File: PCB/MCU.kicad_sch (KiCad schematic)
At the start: 40 parts, among them J1 SWD, Q7 2N7002, Q8 2N7002, Q9 2N7002, SW66 Reset, U2 W25Q128JVS, U3 RP2040, U7 SN74AHCT1G125, Y1 12MHz

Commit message: Large update.
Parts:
- removed C93: 10u, Capacitor_SMD:C_0603_1608Metric, symbol Device:C_Small
- removed C98: 100n, Capacitor_SMD:C_0402_1005Metric, symbol Device:C_Small
- removed D63: 1N4148, Honeydew:D_SOD-323, symbol Device:D_Small
- removed Q7, Q8, Q9: 2N7002, Package_TO_SOT_SMD:SOT-23, symbol Transistor_FET:2N7002
- removed R10: 100k, Resistor_SMD:R_0402_1005Metric, symbol Device:R_Small
- removed R10 (x3), R5: 10k, Resistor_SMD:R_0402_1005Metric, symbol Device:R_Small
- removed R15: 1M, Resistor_SMD:R_0402_1005Metric, symbol Device:R_Small
- removed R20: 1k, Resistor_SMD:R_0402_1005Metric, symbol Device:R_Small
- removed R21: 120k, Resistor_SMD:R_0402_1005Metric, symbol Device:R_Small
- added C96: 100n, Capacitor_SMD:C_0402_1005Metric, symbol Device:C_Small
- added D57: 1N4148, Honeydew:D_SOD-323, symbol Device:D_Small
- added R27 (x2): 10k, Resistor_SMD:R_0402_1005Metric, symbol Device:R_Small
- added SW65: Reset, Button_Switch_SMD:SW_SPDT_PCM12, symbol Cantaloupe:SW_SPST_Small
- C10, C5, C6, C9: Voltage (none) -> 50V
- C11, C12, C13, C14, C15, C16, C17, C18, C19, C7, C8, C92: LCSC C1525 -> C307331; Voltage (none) -> 50V
- J1: footprint Honeydew:PinHeader_1x04_P2.54mm_Vertical_SIlkless -> Connector_PinHeader_2.54mm:PinHeader_1x03_P2.54mm_Vertical; symbol Connector_Generic:Conn_01x04 -> Connector_Generic:Conn_01x03
- SW66: footprint Button_Switch_SMD:SW_SPST_TL3342 -> Honeydew:Panasonic_EVQPUL_EVQPUC; LCSC C318884 -> C79174
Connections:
- net +3V3: now also D57.1 (K), R27.1, R27.1; no longer J1.4 (Pin_4), R6.1, SW66.2 (B)
- net DC_OLED: now also U3.38 (GPIO26_ADC0); no longer U3.40 (GPIO28_ADC2)
- net GND: now also SW66.1 (A), C96.1, SW65.1 (A)
- net RX: now also U3.40 (GPIO28_ADC2); no longer U3.38 (GPIO26_ADC0)
- net SS_OLED: now also U3.39 (GPIO27_ADC1); no longer U3.41 (GPIO29_ADC3)
- net TX: now also U3.41 (GPIO29_ADC3); no longer U3.39 (GPIO27_ADC1)
- net ~{RST}: now also SW66.2 (B), C96.2, D57.2 (A), R27.2; no longer R6.2
- net +5V renamed +5VD
- net COL12 renamed COLM
- net Flash_SS: no longer names the net of U2.1 (~{CS}), U3.56 (QSPI_SS)
- net Flash_SS: now also R6.1, R27.2
- new net: R6.2, SW65.2 (B)
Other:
- moved on the sheet: C10, C5, C6, C9, R7, R8, R9, SW66, U2, U3, U7, Y1

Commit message: Added large caps to output of TPS2557. Updated STEP file and file data.
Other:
- company: (none) -> Created by Ariamelon (https://github.com/Ariamelon/Honeydew/)
- title: (none) -> Honeydew unified split ergonomic keyboard
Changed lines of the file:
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@@
   (paper "A4")
   (title_block
-    (date "2023-04-03")
+    (title "Honeydew unified split ergonomic keyboard")
+    (date "2023-04-08")
     (rev "V2.0")
+    (company "Created by Ariamelon (https://github.com/Ariamelon/Honeydew/)")
     (comment 1 "All capacitors 50V unless otherwise specified.")
+    (comment 2 "Licensed under CC BY 4.0.")
   )
   (junction (at 146.05 31.75) (diameter 0) (color 0 0 0 0)

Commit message: Added plate DXF and gerbers. Removed split comms ports and ideal diode.
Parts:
- SW66: LCSC C79174 -> C110293
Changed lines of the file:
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@@
       (effects (font (size 1.27 1.27)) hide)
     )
-    (property "LCSC" "C79174" (at 181.61 85.09 0)
+    (property "LCSC" "C110293" (at 181.61 85.09 0)
       (effects (font (size 1.27 1.27)) hide)
     )

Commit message: 17/04/2023 large update.
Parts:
- removed C11, C92, C96: 100n, Capacitor_SMD:C_0402_1005Metric, symbol Device:C_Small
- removed SW65: Reset, Button_Switch_SMD:SW_SPDT_PCM12, symbol Cantaloupe:SW_SPST_Small
- removed SW66: Reset, Honeydew:Panasonic_EVQPUL_EVQPUC, symbol Cantaloupe:SW_SPST_Small
- removed U7: SN74AHCT1G125, Package_TO_SOT_SMD:SOT-23-5, symbol Honeydew:SN74AHCT1G125
- added C101: 4u7, Capacitor_SMD:C_0603_1608Metric, symbol Device:C_Small
- added C24, C25: 100n, Capacitor_SMD:C_0402_1005Metric, symbol Device:C_Small
- added SW68: Reset, Honeydew:Panasonic_EVQPUL_EVQPUC, symbol Cantaloupe:SW_SPST_Small
- added SW69: BOOT_SEL, Button_Switch_SMD:SW_SPDT_PCM12, symbol Switch:SW_SPDT
- added U3: SN74AHCT1G125, Package_TO_SOT_SMD:SOT-23-5, symbol Honeydew:SN74AHCT1G125
- J1: footprint Connector_PinHeader_2.54mm:PinHeader_1x03_P2.54mm_Vertical -> Honeydew:Header_SWD
- U2: footprint Package_SO:SOIC-8_5.23x5.23mm_P1.27mm -> Honeydew:SOIC-8_5.23x5.23mm_P1.27mm
- renumbered C10 to C11, U3 to U1
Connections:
- net COLM is gone; now on net ROW2: U1.14 (GPIO11)
- net MOTION is gone; now on net ROW4: U1.16 (GPIO13)
- net +3V3: now also C101.2, C25.2
- net GND: now also C101.1, C24.1, C25.1, SW68.1 (A), SW69.2 (B), SW69.3 (C), U3.1 (~{OE}), U3.3 (GND)
- net RGB: now also U3.4 (Y)
- net ROW0: now also U1.12 (GPIO9); no longer U1.8 (GPIO6)
- net ROW1: now also U1.13 (GPIO10); no longer U1.9 (GPIO7)
- net ROW2: no longer U1.11 (GPIO8)
- net ROW3: now also U1.15 (GPIO12); no longer U1.12 (GPIO9)
- net ROW4: no longer U1.13 (GPIO10)
- net ~{RST}: now also C24.2, SW68.2 (B)
- net FLASH_CS: now reaches R27.2, R6.1, U1.56 (QSPI_SS), U2.1 (~{CS})
- net FLASH_SD1: now reaches U1.55 (QSPI_SD1), U2.2 (DO(IO1))
- net FLASH_SD2: now reaches U1.54 (QSPI_SD2), U2.3 (IO2)
- net FLASH_SD0: now reaches U1.53 (QSPI_SD0), U2.5 (DI(IO0))
- net FLASH_CLK: now reaches U1.52 (QSPI_SCLK), U2.6 (CLK)
- net FLASH_SD3: now reaches U1.51 (QSPI_SD3), U2.7 (IO3)
- net at R6.2: now also SW69.1 (A)
- net SWD: now reaches J1.1 (Pin_1), U1.25 (SWD)
- net SWC: now reaches J1.3 (Pin_3), U1.24 (SWCLK)
- net COL0 renamed 1500mA_EN
- net COL1 renamed 3000mA_EN
- net COL10: no longer names the net of U1.3 (GPIO1)
- net COL11 renamed RGB_3V3
- net RGB_3V3: now also U3.2 (A)
- net COL2 renamed OLED_CS
- net COL3 renamed OLED_DC
- net COL4 renamed TB_CS
- net COL5 renamed TB_MOT
- net COL6: no longer names the net of U1.7 (GPIO5)
- net COL7: no longer names the net of U1.6 (GPIO4)
- net COL8: no longer names the net of U1.5 (GPIO3)
- net COL9: no longer names the net of U1.4 (GPIO2)
- net DC_OLED renamed I_SEN
- net RX renamed TUSB_OUT2
- net SS_OLED renamed ILIM_~{FLT}
- net SS_TB renamed MATRIX_CS
- net TX renamed TUSB_OUT1
- new net +5V: U3.5 (VCC)
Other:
- moved on the sheet: C11, J1, R27, R6

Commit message: Rerouting.
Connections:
- net ROTA: now also U1.8 (GPIO6); no longer U1.17 (GPIO14)
- net ROTB: now also U1.9 (GPIO7); no longer U1.18 (GPIO15)
- net ROW0: now also U1.3 (GPIO1); no longer U1.12 (GPIO9)
- net ROW1: now also U1.4 (GPIO2); no longer U1.13 (GPIO10)
- net ROW2: now also U1.5 (GPIO3); no longer U1.14 (GPIO11)
- net ROW3: now also U1.6 (GPIO4); no longer U1.15 (GPIO12)
- net ROW4: now also U1.7 (GPIO5); no longer U1.16 (GPIO13)
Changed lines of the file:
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@@
     (stroke (width 0) (type default))
   )
-  (wire (pts (xy 130.81 76.2) (xy 128.27 76.2))
+  (wire (pts (xy 130.81 55.88) (xy 128.27 55.88))
     (stroke (width 0) (type default))
   )
@@
     (stroke (width 0) (type default))
   )
-  (wire (pts (xy 130.81 71.12) (xy 128.27 71.12))
+  (wire (pts (xy 130.81 50.8) (xy 128.27 50.8))
     (stroke (width 0) (type default))
   )
@@
     (stroke (width 0) (type default))
   )
-  (wire (pts (xy 130.81 86.36) (xy 128.27 86.36))
+  (wire (pts (xy 130.81 66.04) (xy 128.27 66.04))
     (stroke (width 0) (type default))
   )
@@
     (stroke (width 0) (type default))
   )
-  (wire (pts (xy 130.81 83.82) (xy 128.27 83.82))
+  (wire (pts (xy 130.81 63.5) (xy 128.27 63.5))
     (stroke (width 0) (type default))
   )
@@
     (stroke (width 0) (type default))
   )
-  (wire (pts (xy 130.81 73.66) (xy 128.27 73.66))
+  (wire (pts (xy 130.81 53.34) (xy 128.27 53.34))
     (stroke (width 0) (type default))
   )
@@
     (stroke (width 0) (type default))
   )
-  (wire (pts (xy 130.81 78.74) (xy 128.27 78.74))
+  (wire (pts (xy 130.81 58.42) (xy 128.27 58.42))
     (stroke (width 0) (type default))
   )
@@
     (stroke (width 0) (type default))
   )
-  (wire (pts (xy 130.81 81.28) (xy 128.27 81.28))
+  (wire (pts (xy 130.81 60.96) (xy 128.27 60.96))
     (stroke (width 0) (type default))
   )
@@
     )
   )
-  (hierarchical_label "ROW1" (shape input) (at 130.81 73.66 0) (fields_autoplaced)
+  (hierarchical_label "ROW1" (shape input) (at 130.81 53.34 0) (fields_autoplaced)
     (effects (font (size 1.27 1.27)) (justify left))
   )
@@
     (effects (font (size 1.27 1.27)) (justify left))
   )
-  (hierarchical_label "ROW3" (shape input) (at 130.81 78.74 0) (fields_autoplaced)
+  (hierarchical_label "ROW3" (shape input) (at 130.81 58.42 0) (fields_autoplaced)
     (effects (font (size 1.27 1.27)) (justify left))
   )
@@
     (effects (font (size 1.27 1.27)) (justify left))
   )
-  (hierarchical_label "ROTB" (shape output) (at 130.81 86.36 0) (fields_autoplaced)
-    (effects (font (size 1.27 1.27)) (justify left))
-  )
-  (hierarchical_label "ROTA" (shape output) (at 130.81 83.82 0) (fields_autoplaced)
+  (hierarchical_label "ROTB" (shape output) (at 130.81 66.04 0) (fields_autoplaced)
+    (effects (font (size 1.27 1.27)) (justify left))
+  )
+  (hierarchical_label "ROTA" (shape output) (at 130.81 63.5 0) (fields_autoplaced)
     (effects (font (size 1.27 1.27)) (justify left))
   )
@@
     (effects (font (size 1.27 1.27)) (justify left))
   )
-  (hierarchical_label "ROW2" (shape input) (at 130.81 76.2 0) (fields_autoplaced)
+  (hierarchical_label "ROW2" (shape input) (at 130.81 55.88 0) (fields_autoplaced)
     (effects (font (size 1.27 1.27)) (justify left))
   )
@@
     (effects (font (size 1.27 1.27)) (justify left))
   )
-  (hierarchical_label "ROW4" (shape input) (at 130.81 81.28 0) (fields_autoplaced)
+  (hierarchical_label "ROW4" (shape input) (at 130.81 60.96 0) (fields_autoplaced)
     (effects (font (size 1.27 1.27)) (justify left))
   )
@@
     (effects (font (size 1.27 1.27)) (justify left))
   )
-  (hierarchical_label "ROW0" (shape input) (at 130.81 71.12 0) (fields_autoplaced)
-    (effects (font (size 1.27 1.27)) (justify left))
-  )
+  (hierarchical_label "ROW0" (shape input) (at 130.81 50.8 0) (fields_autoplaced)
+    (effects (font (size 1.27 1.27)) (justify left))
+  )

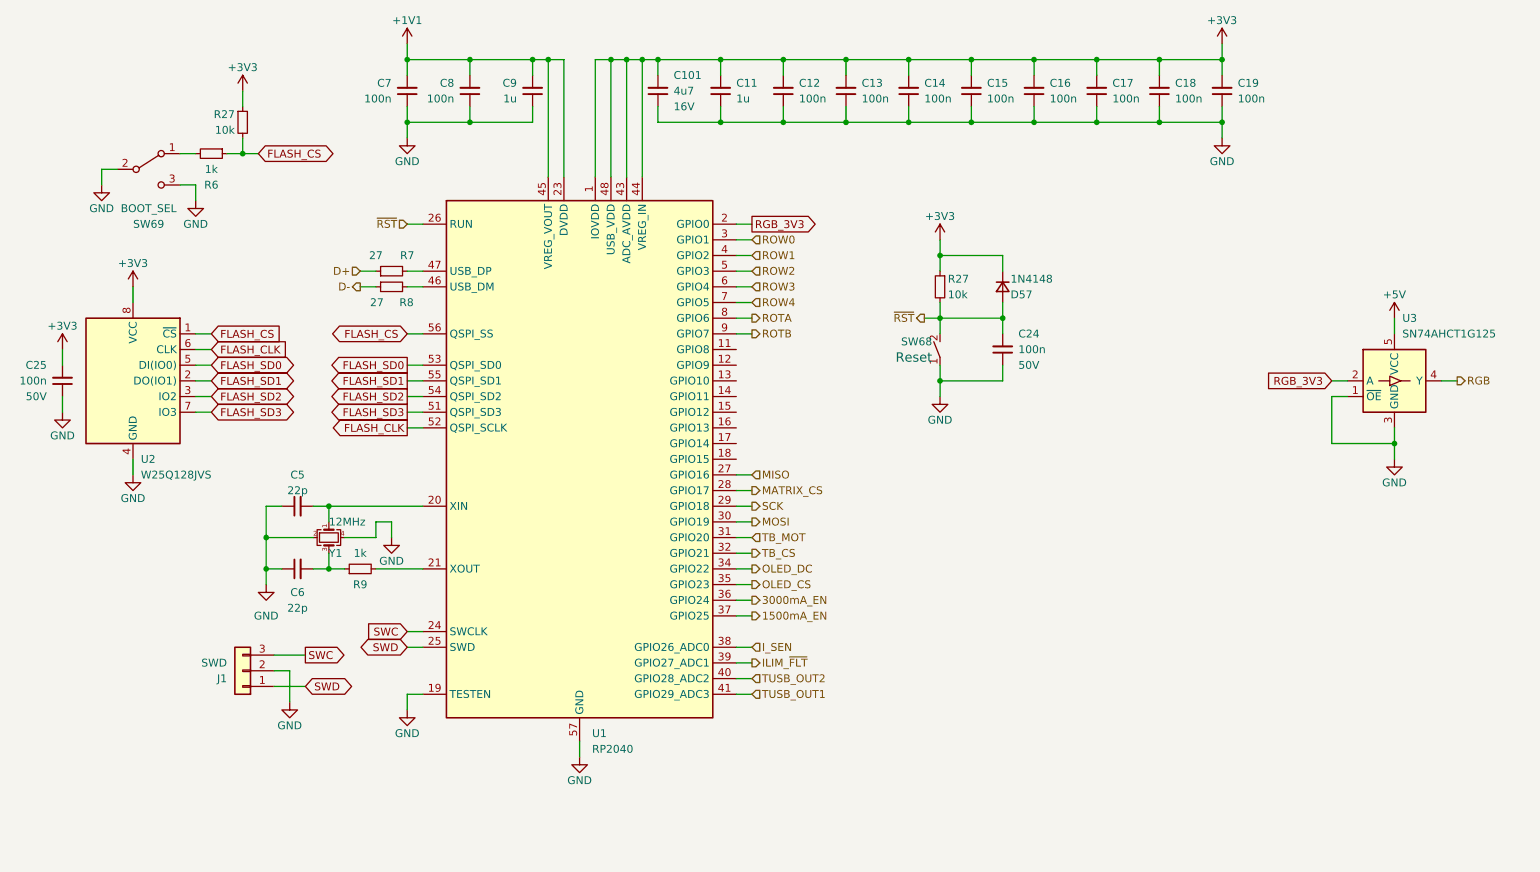
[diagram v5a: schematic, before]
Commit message: 3/4-done update.
Added current and voltage measurement for VBUS in and current measurement for the RGB output. Added PMOS power switch to fully turn off RGB LEDs when not in use. Rerouted the PCB. Moved OLED ribbon cable cutout and expanded it length-wise. Changed position of various components for better routing. Changed bulk capacitance of RGB LEDs to 5 x 22u capacitors. Changed the four N mosfets to two much smaller dual N mosfets. Still need to do RGB routing!
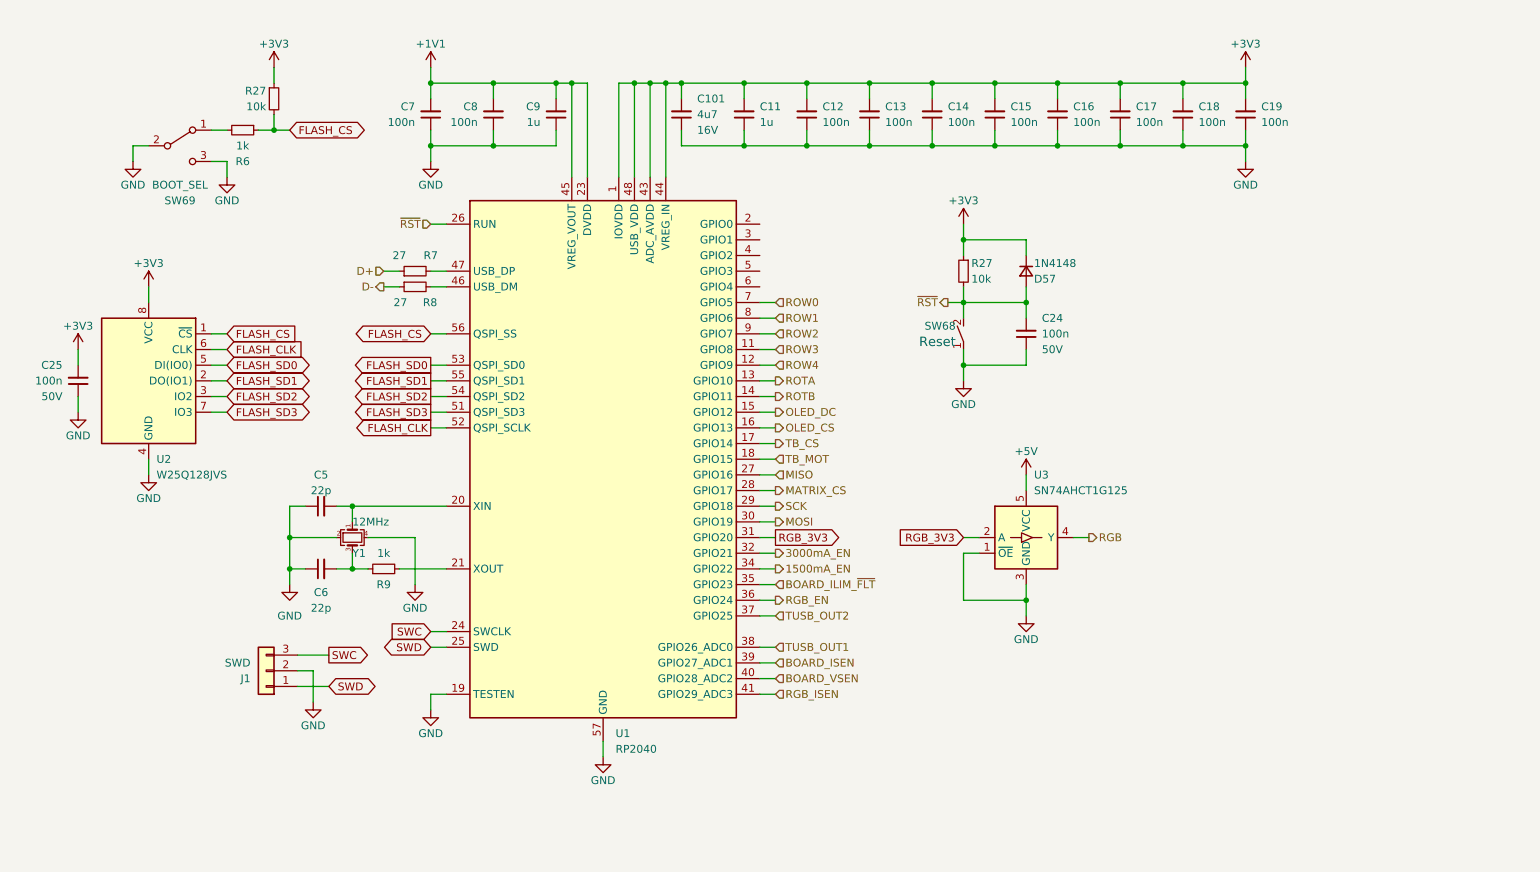
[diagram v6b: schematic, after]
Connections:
- net I_SEN is gone; now on net TUSB_OUT1: U1.38 (GPIO26_ADC0)
- net 1500mA_EN: now also U1.34 (GPIO22); no longer U1.37 (GPIO25)
- net 3000mA_EN: now also U1.32 (GPIO21); no longer U1.36 (GPIO24)
- net OLED_CS: now also U1.16 (GPIO13); no longer U1.35 (GPIO23)
- net OLED_DC: now also U1.15 (GPIO12); no longer U1.34 (GPIO22)
- net RGB_3V3: now also U1.31 (GPIO20); no longer U1.2 (GPIO0)
- net ROTA: now also U1.13 (GPIO10); no longer U1.8 (GPIO6)
- net ROTB: now also U1.14 (GPIO11); no longer U1.9 (GPIO7)
- net ROW0: now also U1.7 (GPIO5); no longer U1.3 (GPIO1)
- net ROW1: now also U1.8 (GPIO6); no longer U1.4 (GPIO2)
- net ROW2: now also U1.9 (GPIO7); no longer U1.5 (GPIO3)
- net ROW3: now also U1.11 (GPIO8); no longer U1.6 (GPIO4)
- net ROW4: now also U1.12 (GPIO9); no longer U1.7 (GPIO5)
- net TB_CS: now also U1.17 (GPIO14); no longer U1.32 (GPIO21)
- net TB_MOT: now also U1.18 (GPIO15); no longer U1.31 (GPIO20)
- net TUSB_OUT1: no longer U1.41 (GPIO29_ADC3)
- net TUSB_OUT2: now also U1.37 (GPIO25); no longer U1.40 (GPIO28_ADC2)
- net ILIM_~{FLT} renamed BOARD_ISEN
- new net BOARD_ILIM_~{FLT}: U1.35 (GPIO23)
- new net BOARD_VSEN: U1.40 (GPIO28_ADC2)
- new net RGB_EN: U1.36 (GPIO24)
- new net RGB_ISEN: U1.41 (GPIO29_ADC3)
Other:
- moved on the sheet: C101, C11, C12, C13, C14, C15, C16, C17, C18, C19, C24, C25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

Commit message: BLE version incomplete update.
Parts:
- removed C101: 4u7, Capacitor_SMD:C_0603_1608Metric, symbol Device:C_Small
- removed C12, C13, C14, C15, C16, C17, C18, C19, C25, C7, C8: 100n, Capacitor_SMD:C_0402_1005Metric, symbol Device:C_Small
- removed C9: 1u, Capacitor_SMD:C_0603_1608Metric, symbol Device:C_Small
- removed J1: SWD, Honeydew:Header_SWD, symbol Connector_Generic:Conn_01x03
- removed R27 (x2): 10k, Resistor_SMD:R_0402_1005Metric, symbol Device:R_Small
- removed R6, R9: 1k, Resistor_SMD:R_0402_1005Metric, symbol Device:R_Small
- removed R7, R8: 27, Resistor_SMD:R_0402_1005Metric, symbol Device:R_Small
- removed SW69: BOOT_SEL, Button_Switch_SMD:SW_SPDT_PCM12, symbol Switch:SW_SPDT
- removed U1: RP2040, Honeydew:QFN-56-1EP_7x7mm_P0.4mm_EP3.2x3.2mm_ThermalVias, symbol MCU_RaspberryPi:RP2040
- removed U2: W25Q128JVS, Honeydew:SOIC-8_5.23x5.23mm_P1.27mm, symbol Memory_Flash:W25Q128JVS
- removed U3: SN74AHCT1G125, Package_TO_SOT_SMD:SOT-23-5, symbol Honeydew:SN74AHCT1G125
- removed Y1: 12MHz, Crystal:Crystal_SMD_3225-4Pin_3.2x2.5mm, symbol Device:Crystal_GND24_Small
- added C28: 100n, Capacitor_SMD:C_0402_1005Metric, symbol Device:C_Small
- added C31: 4u7, Capacitor_SMD:C_0603_1608Metric, symbol Device:C_Small
- added C39 (x2): 10u, Capacitor_SMD:C_0603_1608Metric, symbol Device:C_Small
- added D65: SK6805, LED_SMD:LED_SK6805_PLCC4_2.4x2.7mm_P1.3mm, symbol LED:SK6805
- added J6: SWD, Connector_PinHeader_1.27mm:PinHeader_2x05_P1.27mm_Vertical, symbol Connector_Generic:Conn_02x05_Odd_Even
- added Q1: BSS138BKS, Package_TO_SOT_SMD:SOT-363_SC-70-6, symbol Device:Q_Dual_NMOS_S1G1D2S2G2D1
- added Q4: AON7407, Honeydew:AO_DFN-8-3x3, symbol Transistor_FET:AON6411
- added R16: 1k, Resistor_SMD:R_0402_1005Metric, symbol Device:R_Small
- added R32 (x2): 10k, Resistor_SMD:R_0402_1005Metric, symbol Device:R_Small
- added U1: MDBT50Q-U1MV2, RF_Module:Raytac_MDBT50Q, symbol Honeydew:MDBT50Q
- added U3: W25Q128JW, Package_SON:WSON-8-1EP_6x5mm_P1.27mm_EP3.4x4.3mm, symbol Memory_Flash:W25Q32JVZP
- added U6: SN74LV1T34, Package_TO_SOT_SMD:SOT-353_SC-70-5, symbol Logic_LevelTranslator:SN74LV1T34DCK
- added Y1: 32.768k, Crystal:Crystal_SMD_3215-2Pin_3.2x1.5mm, symbol Device:Crystal_Small
- C11: value 1u -> 100n; footprint Capacitor_SMD:C_0603_1608Metric -> Capacitor_SMD:C_0402_1005Metric; LCSC C15849 -> C307331
- C5, C6: value 22p -> 15p; LCSC C1555 -> C1548
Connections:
- net GND: now also C28.1, C39.2, C39.2, D65.2 (VSS), J6.3 (Pin_3), J6.5 (Pin_5), J6.9 (Pin_9), Q1.4 (S), U1.1 (GND), U1.15 (GND), U1.2 (GND), U1.33 (GND), U1.55 (GND), U3.4 (GND), U3.9 (EP), U6.3 (GND)
- net RGB_EN: now also Q1.5 (G)
- net ~{RST}: now also J6.10 (Pin_10), R32.2, U1.40 (~{RESET}/P0.18)
- net at C6.2: now also U1.18 (XL2/P0.01), Y1.1
- net at C5.2: now also U1.17 (XL1/P0.00), Y1.2
- net +3V3 renamed VDD
- net VDD: now also C39.1, J6.1 (Pin_1), R32.1, U1.28 (VDD), U1.30 (VDDH), U3.8 (VCC)
- new net: D65.3 (DIN), U6.4 (Y)
- new net: C31.1, Q4.4 (G), R16.1, R32.2
- new net: Q1.3 (D), R16.2
- new net MCU_D+: U1.35 (D+)
- new net MCU_D-: U1.34 (D-)
- new net QSPI_D0: U1.41 (P0.17), U3.5 (DI(IO0))
- new net QSPI_D1: U1.46 (P0.22), U3.2 (DO(IO1))
- new net QSPI_D2: U1.45 (P0.23), U3.3 (IO2)
- new net QSPI_D3: U1.43 (P0.21), U3.7 (IO3)
- new net QSPI_SCK: U1.42 (P0.19), U3.6 (CLK)
- new net QSPI_~{CS}: U1.44 (P0.20), U3.1 (~{CS})
- new net RGB_EXT: D65.1 (DOUT)
- new net RGB_NRF: U6.2 (A)
- new net SWCLK: J6.4 (Pin_4), U1.53 (SWDCLK)
- new net SWDIO: J6.2 (Pin_2), U1.51 (SWDIO)
- new net VBUS: C39.1, U1.32 (VBUS)
- new net VEXT: C28.2, C31.2, D65.4 (VDD), Q4.5 (D), U6.5 (VCC)
- new net VSYS: Q4.1 (S), Q4.2 (S), Q4.3 (S), R32.1
- no-connect marks 0 -> 4
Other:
- moved on the sheet: C24, D57, SW68
